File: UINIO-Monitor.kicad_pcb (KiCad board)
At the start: 2 copper layers, 0 parts

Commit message: Finish drawing the board frame.
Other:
- board outline added: 66.3 x 77.9 mm

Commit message: Complete schematic drawing.
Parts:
- added C1: C, Capacitor_SMD:C_0603_1608Metric, F.Cu at (219.4, 95.5)
- added C10: C, Capacitor_SMD:C_0402_1005Metric, F.Cu at (240.5, 77.0)
- added C11: C, Capacitor_SMD:C_0402_1005Metric, F.Cu at (222.9, 94.3)
- added C12: C, Capacitor_SMD:C_0402_1005Metric, F.Cu at (236.5, 79.5)
- added C13: C, Capacitor_SMD:C_0402_1005Metric, F.Cu at (231.5, 86.8)
- added C2: C, Capacitor_SMD:C_0603_1608Metric, F.Cu at (224.0, 89.6)
- added C3: C, Capacitor_SMD:C_0603_1608Metric, F.Cu at (228.1, 87.0)
- added C4: C, Capacitor_SMD:C_0603_1608Metric, F.Cu at (237.1, 77.2)
- added C5: C, Capacitor_SMD:C_0603_1608Metric, F.Cu at (193.5, 105.5)
- added C6: C, Capacitor_SMD:C_0603_1608Metric, F.Cu at (219.4, 93.0)
- added C7: C, Capacitor_SMD:C_0603_1608Metric, F.Cu at (224.0, 87.0)
- added C8: C, Capacitor_SMD:C_0402_1005Metric, F.Cu at (227.5, 89.3)
- added C9: C, Capacitor_SMD:C_0402_1005Metric, F.Cu at (217.4, 101.3)
- added D1: 1N4148W, Diode_SMD:D_SOD-123, F.Cu at (190.3, 102.6)
- added FPC1: FPC-SMD_10P-0.5mm, Uinio:FPC-SMD_KH-FG0.5-H2.0-10Pin, F.Cu at (211.9, 93.2)
- added FPC2: FPC-SMD_10P-0.5mm, Uinio:FPC-SMD_KH-FG0.5-H2.0-10Pin, F.Cu at (202.2, 103.4)
- added J1: Conn_01x09_Male, Connector_PinHeader_2.54mm:PinHeader_1x09_P2.54mm_Vertical, F.Cu at (194.4, 78.3)
- added J2: Conn_01x09_Male, Connector_PinHeader_2.54mm:PinHeader_1x09_P2.54mm_Vertical, F.Cu at (189.8, 78.3)
- added J3: Conn_01x04_Male, Connector_PinHeader_2.54mm:PinHeader_1x04_P2.54mm_Vertical, F.Cu at (208.8, 78.3)
- added P1: LCD_Pad_10Pin, Uinio:LCD_Pad_10Pin, F.Cu at (165.0, 73.5)
- added P2: LCD_Pad_12Pin, Uinio:LCD_Pad_12Pin, F.Cu at (134.9, 125.7)
- added P3: OLED_Pad_30Pin, Uinio:OLED_Pad_30Pin, F.Cu at (163.6, 126.0)
- added R1: R, Resistor_SMD:R_0603_1608Metric, F.Cu at (189.4, 105.5)
- added R10: R, Resistor_SMD:R_0402_1005Metric, F.Cu at (213.4, 103.8)
- added R2: R, Resistor_SMD:R_0603_1608Metric, F.Cu at (232.5, 81.8)
- added R3: R, Resistor_SMD:R_0603_1608Metric, F.Cu at (236.5, 81.8)
- added R4: R, Resistor_SMD:R_0603_1608Metric, F.Cu at (224.0, 92.1)
- added R5: R, Resistor_SMD:R_0603_1608Metric, F.Cu at (232.5, 84.3)
- added R6: R, Resistor_SMD:R_0603_1608Metric, F.Cu at (214.0, 101.6)
- added R7: R, Resistor_SMD:R_0402_1005Metric, F.Cu at (194.7, 101.9)
- added R8: R, Resistor_SMD:R_0402_1005Metric, F.Cu at (209.2, 105.8)
- added R9: R, Resistor_SMD:R_0402_1005Metric, F.Cu at (218.6, 97.8)
- added U1: ME6211, Uinio:SOT-23-5_L3.0-W1.7-P0.95-LS2.8-BR, F.Cu at (219.7, 89.4)
- added U2: ME6211, Uinio:SOT-23-5_L3.0-W1.7-P0.95-LS2.8-BR, F.Cu at (232.8, 78.1)
- added U3: XC6206PxxxMR, Package_TO_SOT_SMD:SOT-23-3, F.Cu at (210.3, 98.0)
- added VT1: S8050, Uinio:SOT-23-3_L2.9-W1.6-P1.90-LS2.9-BL, F.Cu at (215.0, 98.0)
- added VT2: S8050, Uinio:SOT-23-3_L2.9-W1.6-P1.90-LS2.9-BL, F.Cu at (209.9, 102.4)

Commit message: Update footprint.
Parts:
- moved P3 2.97 mm to (164.0, 128.9)

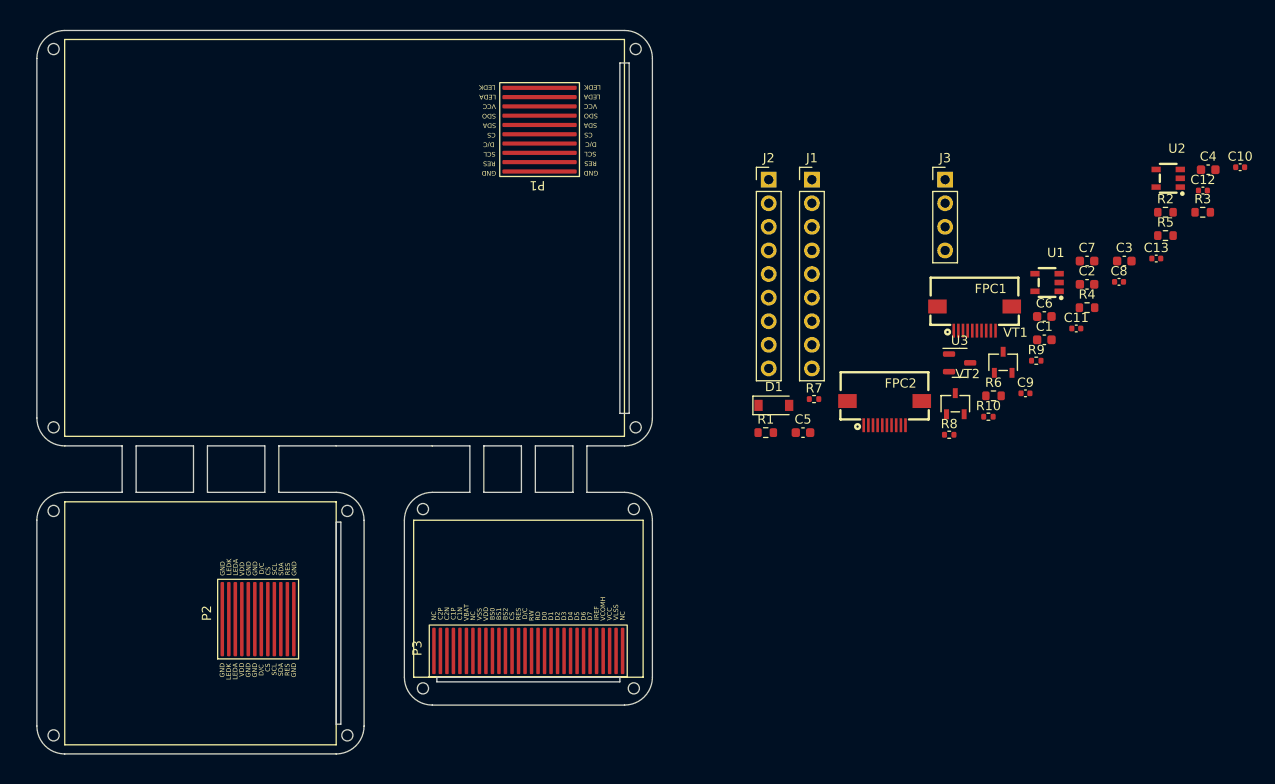
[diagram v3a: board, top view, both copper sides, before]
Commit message: Complete component layout.
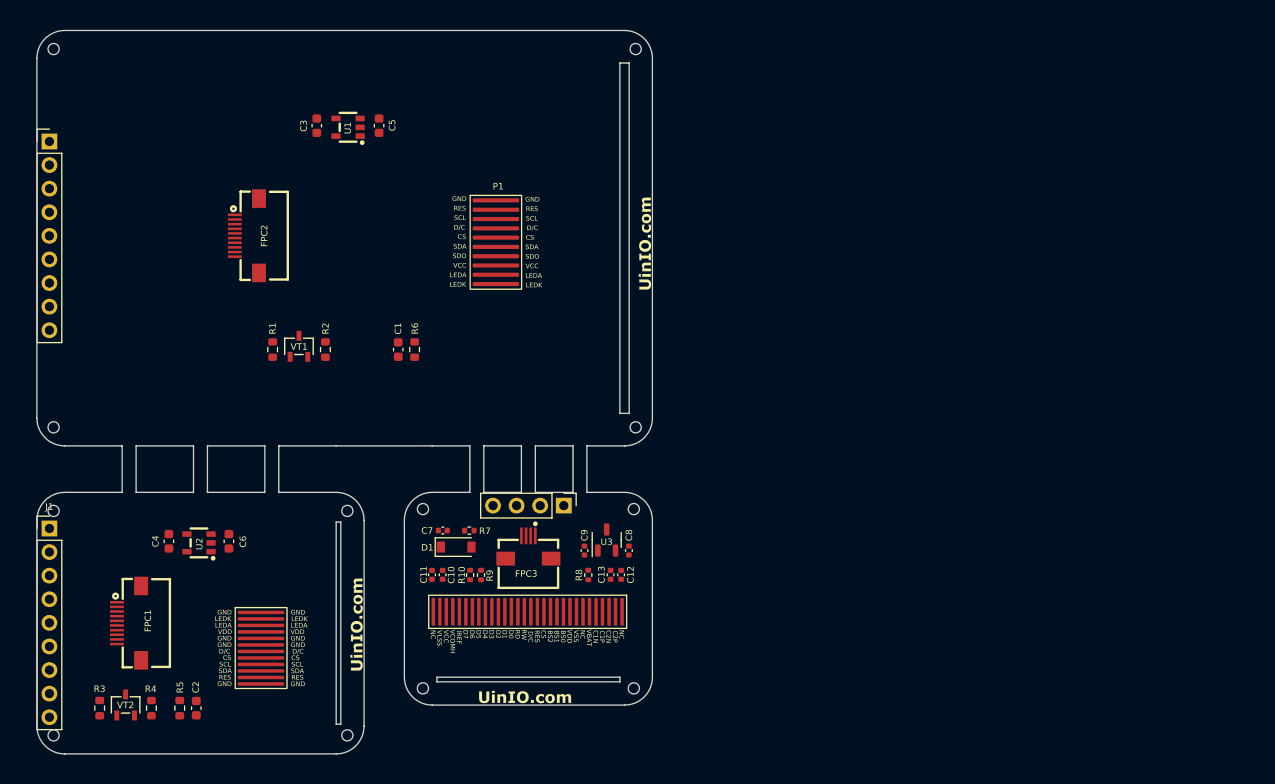
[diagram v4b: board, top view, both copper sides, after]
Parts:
- added ?: LOGO, LOGO, F.Cu at (163.5, 134.0)
- added ?: LOGO, LOGO, F.Cu at (145.4, 126.2)
- added ?: LOGO, LOGO, F.Cu at (176.4, 85.2)
- added ?: LOGO, LOGO, B.Cu at (164.2, 123.3)
- added ?: LOGO, LOGO, B.Cu at (128.5, 126.4)
- added ?: LOGO, LOGO, B.Cu at (143.8, 85.2)
- added FPC3: FPC-SMD_4P-0.5mm, Uinio:FPC-SMD_4P-P0.5, F.Cu at (163.9, 117.9)
- C1, C12, C13, C2, C3, C4, C5, C6, C8: value C -> 1uF
- C10: value C -> 4.7uF
- C11: value C -> 2.2uF
- C7: value C -> 0.1uF; footprint Capacitor_SMD:C_0603_1608Metric -> Capacitor_SMD:C_0402_1005Metric
- C9: value C -> 0.1uF
- R1, R3: value R -> 1K
- R10: value R -> 910K
- R2, R4, R7, R8, R9: value R -> 10K
- R5, R6: value R -> 10R
- moved R3 130.2 mm to (117.8, 135.2), turned to 90 degrees
- moved C4 118.8 mm to (125.2, 117.2), turned to 90 degrees
- moved R5 117.7 mm to (126.4, 135.2), turned to -90 degrees
- moved U2 111.5 mm to (128.4, 117.4)
- moved R4 109.6 mm to (123.3, 135.2), turned to -90 degrees
- moved C2 106.2 mm to (128.2, 135.2), turned to -90 degrees
- moved FPC1 96.7 mm to (120.9, 126.0), turned to -90 degrees
- moved C10 96.4 mm to (154.7, 120.8), turned to 90 degrees
- moved VT2 95.0 mm to (120.5, 134.8)
- moved R2 91.6 mm to (142.1, 96.6), turned to -90 degrees
- moved C6 91.1 mm to (131.7, 117.2), turned to -90 degrees
- moved J1 90.3 mm to (112.3, 115.8)
- moved C3 88.1 mm to (141.1, 72.5), turned to 90 degrees
- moved J2 77.5 mm to (112.3, 74.2)
- moved U1 77.1 mm to (144.5, 72.7)
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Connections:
- R1 pad 1: /3.3V_2.4inch -> /BLK_2.4inch
- R2 pad 2: /BLK_2.4inch -> /3.3V_2.4inch
- R7 pad 1: /SCK_0.96inch -> /RESET_0.96inch
- R8 pad 1: /SDA_0.96inch -> /SCK_0.96inch
- R9 pad 1: /RESET_0.96inch -> /SDA_0.96inch

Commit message: Update footprint.
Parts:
- moved FPC2 7.57 mm to (141.2, 84.7)
- moved C4 4.86 mm to (120.3, 117.2)
- moved C6 4.86 mm to (126.8, 117.2)
- moved U2 4.86 mm to (123.6, 117.4)
- moved C1 2.87 mm to (147.0, 96.3)
- moved R6 2.87 mm to (148.8, 96.3)
- moved U1 1.83 mm to (142.7, 73.2)
- moved C3 1.82 mm to (139.4, 73.0)
- moved C5 1.82 mm to (146.1, 73.0)
- moved FPC1 0.95 mm to (121.9, 126.0)
- moved R4 0.80 mm to (124.1, 135.2)
- moved R3 0.80 mm to (118.5, 135.2)
- moved R5 0.80 mm to (127.2, 135.2)
- moved VT2 0.80 mm to (121.3, 134.8)
- moved C2 0.80 mm to (128.9, 135.2)
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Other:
- outline, holes or cut-outs redrawn
- board text added: "0.96英寸 I²C接口"
- board text added: "1.33英寸 SPI接口"
- board text added: "2.4英寸 SPI接口"
- board text added: "3V3"
- board text added: "5V"
- board text added: "BLK"
- board text added: "CS"
- board text added: "D/C"
- board text added: "GND"
- board text added: "RST"
- board text added: "SCK"
- board text added: "SCL"
- board text added: "SDA"
- board text added: "UINIO-Monitor"
- board text added: "VCC"
- board text added: "屏幕驱动芯片：SSD1315"
- board text added: "屏幕驱动芯片：ST7789"

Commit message: Update footprint.
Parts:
- moved P3 1.05 mm to (163.8, 123.8)
- moved C13 1.04 mm to (171.8, 120.3)
- moved R10 0.98 mm to (156.9, 120.1)
- moved R9 0.84 mm to (158.9, 120.1)
- moved C10 0.80 mm to (154.8, 120.1)
- moved C11 0.80 mm to (153.7, 120.1)
- moved FPC3 0.73 mm to (163.9, 117.1)
- moved R8 0.70 mm to (169.9, 120.3)
- moved D1 0.55 mm to (155.9, 117.3)
- moved C7 0.55 mm to (154.5, 115.5)
- moved R7 0.55 mm to (157.4, 115.5)
- moved C12 0.54 mm to (173.8, 120.3)
- moved U3 0.50 mm to (172.3, 116.6)
- moved C8 0.50 mm to (174.7, 117.7)
- moved C9 0.50 mm to (169.9, 117.7)
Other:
- board text added: "屏幕驱动：ST7789"
- board text removed: "屏幕驱动芯片：ST7789"

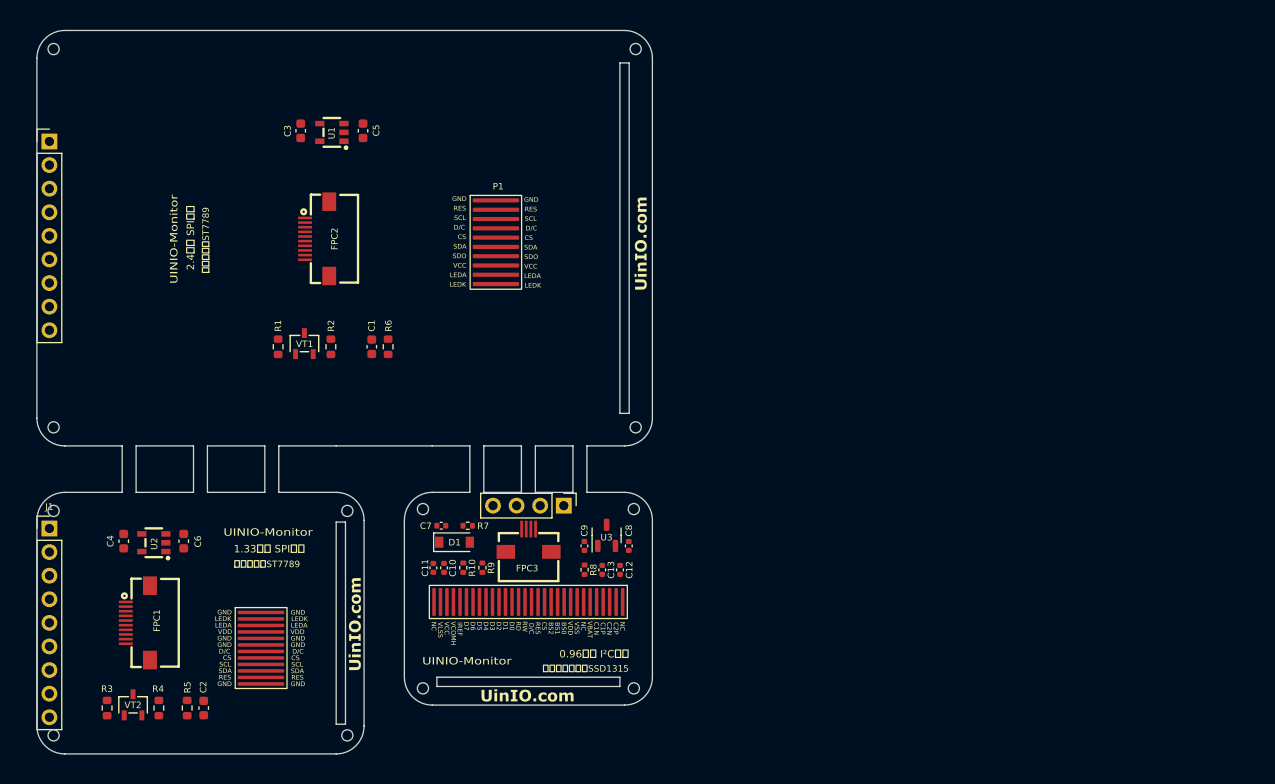
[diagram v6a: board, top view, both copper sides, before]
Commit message: Complete PCB routing.
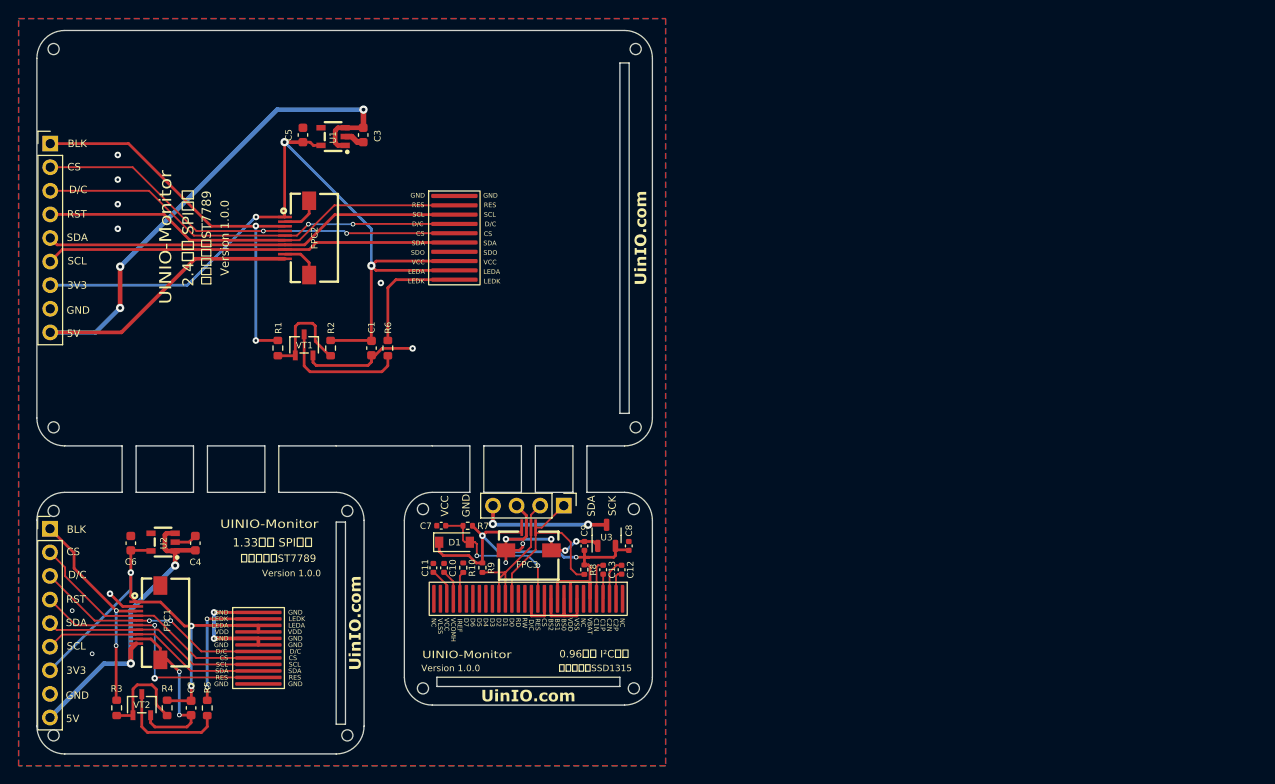
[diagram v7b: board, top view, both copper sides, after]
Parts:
- moved C4 7.71 mm to (128.1, 117.4), turned to -90 degrees
- moved C3 6.75 mm to (146.1, 73.5)
- moved C5 6.49 mm to (139.6, 73.5)
- moved C6 5.70 mm to (121.1, 117.4)
- moved P1 4.50 mm to (156.0, 83.9)
- moved FPC2 2.16 mm to (139.0, 84.6)
- moved R5 2.16 mm to (129.3, 135.2), turned to 90 degrees
- moved C2 1.36 mm to (127.6, 135.2), turned to 90 degrees
- moved FPC1 1.12 mm to (123.0, 126.0)
- moved R3 1.03 mm to (119.6, 135.2)
- moved U2 1.00 mm to (124.6, 117.3)
- moved VT2 0.94 mm to (122.3, 134.8)
- moved R4 0.89 mm to (125.0, 135.2)
- moved ? 0.61 mm to (175.9, 84.6)
- moved U1 0.47 mm to (142.9, 73.7)
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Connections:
- C8 pad 2: Net-(C8-Pad2) -> /3.3V_0.96inch
- C9 pad 2: Net-(C8-Pad2) -> /3.3V_0.96inch
- D1 pad 1: Net-(C8-Pad2) -> /3.3V_0.96inch
- FPC1 pad 7: /SDA_1.3inch -> /SCL_1.3inch
- FPC1 pad 8: /SCL_1.3inch -> /SDA_1.3inch
- FPC2 pad 7: /SDA_2.4inch -> /SCL_2.4inch
- FPC2 pad 8: /SCL_2.4inch -> /SDA_2.4inch
- FPC3 pad 4: /VCC_0.96inch -> /3.3V_0.96inch
- J1 pad 5: /SDA_1.3inch -> /SCL_1.3inch
- J1 pad 6: /SCL_1.3inch -> /SDA_1.3inch
- J2 pad 5: /SDA_2.4inch -> /SCL_2.4inch
- J2 pad 6: /SCL_2.4inch -> /SDA_2.4inch
- P3 pad 11: Net-(C8-Pad2) -> /3.3V_0.96inch
- P3 pad 6: Net-(C8-Pad2) -> /3.3V_0.96inch
- P3 pad 9: Net-(C8-Pad2) -> /3.3V_0.96inch
- R7 pad 2: Net-(C8-Pad2) -> /3.3V_0.96inch
- R8 pad 2: Net-(C8-Pad2) -> /3.3V_0.96inch
- R9 pad 2: Net-(C8-Pad2) -> /3.3V_0.96inch
- U3 pad 2: Net-(C8-Pad2) -> /3.3V_0.96inch
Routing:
- net GND: track 0.00 -> 97.9 mm, vias 0 -> 19
- net /3.3V_2.4inch: track 0.00 -> 88.3 mm, vias 0 -> 3
- net /5V_2.4inch: track 0.00 -> 82.4 mm, vias 0 -> 3
- net /CS_2.4inch: track 0.00 -> 48.8 mm, vias 0 -> 2
- net /3.3V_0.96inch: track 0.00 -> 48.3 mm, vias 0 -> 2
- net /3.3V_1.3inch: track 0.00 -> 47.5 mm, vias 0 -> 3
- net /RESET_2.4inch: track 0.00 -> 46.2 mm
- net /D/C_2.4inch: track 0.00 -> 46.0 mm, vias 0 -> 2
- net /SCL_2.4inch: track 0.00 -> 45.2 mm
- net /SDA_2.4inch: track 0.00 -> 44.4 mm
- net /BLK_2.4inch: track 0.00 -> 43.7 mm, vias 0 -> 2
- net /5V_1.3inch: track 0.00 -> 33.7 mm, vias 0 -> 2
- net /RESET_1.3inch: track 0.00 -> 29.3 mm, vias 0 -> 2
- net /CS_1.3inch: track 0.00 -> 27.7 mm
- net /D/C_1.3inch: track 0.00 -> 25.7 mm, vias 0 -> 2
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- added copper zone on B.Cu, net GND
- added copper zone on F.Cu, net GND
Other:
- board text added: "0.96英寸 I²C总线"
- board text added: "1.33英寸 SPI总线"
- board text added: "2.4英寸 SPI总线"
- board text added: "Version 1.0.0"
- board text added: "屏幕驱动：SSD1315"
- board text removed: "0.96英寸 I²C接口"
- board text removed: "1.33英寸 SPI接口"
- board text removed: "2.4英寸 SPI接口"
- board text removed: "屏幕驱动芯片：SSD1315"
